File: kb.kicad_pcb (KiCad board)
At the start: 2 copper layers, 203.2 x 106.4 mm, 182 parts, among them J1 Conn_01x04_Female, J2 10029449-001RLF, SW1 RotaryEncoder_Switch, U1 Pico, U2 SN74AHCT125D

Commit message: fixing sk6812s
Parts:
- moved J1 13.1 mm to (87.6, 37.9)
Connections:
- D101 pad 1: Net-(D101-Pad1) -> +5V
- D101 pad 2: GND -> Net-(D101-Pad2)
- D101 pad 3: /RGB_5V -> GND
- D101 pad 4: +5V -> /RGB_5V
- D102 pad 1: Net-(D102-Pad1) -> +5V
- D102 pad 2: GND -> Net-(D102-Pad2)
- D102 pad 3: Net-(D101-Pad1) -> GND
- D102 pad 4: +5V -> Net-(D101-Pad2)
- D103 pad 1: Net-(D103-Pad1) -> +5V
- D103 pad 2: GND -> Net-(D103-Pad2)
- D103 pad 3: Net-(D102-Pad1) -> GND
- D103 pad 4: +5V -> Net-(D102-Pad2)
- D104 pad 1: Net-(D104-Pad1) -> +5V
- D104 pad 2: GND -> Net-(D104-Pad2)
- D104 pad 3: Net-(D103-Pad1) -> GND
- D104 pad 4: +5V -> Net-(D103-Pad2)
- D105 pad 1: Net-(D105-Pad1) -> +5V
- D105 pad 2: GND -> Net-(D105-Pad2)
- D105 pad 3: Net-(D104-Pad1) -> GND
- D105 pad 4: +5V -> Net-(D104-Pad2)
- D106 pad 1: Net-(D106-Pad1) -> +5V
- D106 pad 2: GND -> Net-(D106-Pad2)
- D106 pad 3: Net-(D105-Pad1) -> GND
- D106 pad 4: +5V -> Net-(D105-Pad2)
- D107 pad 1: Net-(D107-Pad1) -> +5V
- D107 pad 2: GND -> Net-(D107-Pad2)
- D107 pad 3: Net-(D106-Pad1) -> GND
- D107 pad 4: +5V -> Net-(D106-Pad2)
- D108 pad 1: Net-(D108-Pad1) -> +5V
- D108 pad 2: GND -> Net-(D108-Pad2)
- D108 pad 3: Net-(D107-Pad1) -> GND
- D108 pad 4: +5V -> Net-(D107-Pad2)
- D109 pad 1: Net-(D109-Pad1) -> +5V
- D109 pad 2: GND -> Net-(D109-Pad2)
- D109 pad 3: Net-(D109-Pad3) -> GND
- D109 pad 4: +5V -> Net-(D109-Pad4)
- D110 pad 1: Net-(D110-Pad1) -> +5V
- D110 pad 2: GND -> Net-(D110-Pad2)
- D110 pad 3: Net-(D109-Pad1) -> GND
- D110 pad 4: +5V -> Net-(D109-Pad2)
- D111 pad 1: Net-(D111-Pad1) -> +5V
- D111 pad 2: GND -> Net-(D111-Pad2)
- D111 pad 3: Net-(D110-Pad1) -> GND
- D111 pad 4: +5V -> Net-(D110-Pad2)
- D112 pad 1: Net-(D112-Pad1) -> +5V
- D112 pad 2: GND -> Net-(D112-Pad2)
- D112 pad 3: Net-(D111-Pad1) -> GND
- D112 pad 4: +5V -> Net-(D111-Pad2)
- D113 pad 1: Net-(D113-Pad1) -> +5V
- D113 pad 2: GND -> Net-(D113-Pad2)
- D113 pad 3: Net-(D112-Pad1) -> GND
- D113 pad 4: +5V -> Net-(D112-Pad2)
- D114 pad 1: Net-(D114-Pad1) -> +5V
- D114 pad 2: GND -> Net-(D114-Pad2)
- D114 pad 3: Net-(D113-Pad1) -> GND
- D114 pad 4: +5V -> Net-(D113-Pad2)
- D115 pad 1: Net-(D115-Pad1) -> +5V
- D115 pad 2: GND -> Net-(D115-Pad2)
- D115 pad 3: Net-(D114-Pad1) -> GND
- D115 pad 4: +5V -> Net-(D114-Pad2)
- D116 pad 1: Net-(D116-Pad1) -> +5V
- D116 pad 2: GND -> Net-(D116-Pad2)
- D116 pad 3: Net-(D115-Pad1) -> GND
- D116 pad 4: +5V -> Net-(D115-Pad2)
- D117 pad 1: Net-(D117-Pad1) -> +5V
- D117 pad 2: GND -> Net-(D117-Pad2)
- D117 pad 3: Net-(D116-Pad1) -> GND
- D117 pad 4: +5V -> Net-(D116-Pad2)
- D118 pad 1: Net-(D118-Pad1) -> +5V
- D118 pad 2: GND -> Net-(D118-Pad2)
- D118 pad 3: Net-(D117-Pad1) -> GND
- D118 pad 4: +5V -> Net-(D117-Pad2)
- D119 pad 1: Net-(D119-Pad1) -> +5V
- D119 pad 2: GND -> Net-(D119-Pad2)
- D119 pad 3: Net-(D118-Pad1) -> GND
- D119 pad 4: +5V -> Net-(D118-Pad2)
- D120 pad 1: Net-(D120-Pad1) -> +5V
- D120 pad 2: GND -> Net-(D120-Pad2)
- D120 pad 3: Net-(D119-Pad1) -> GND
- D120 pad 4: +5V -> Net-(D119-Pad2)
- D121 pad 1: Net-(D121-Pad1) -> +5V
- D121 pad 2: GND -> Net-(D121-Pad2)
- D121 pad 3: Net-(D120-Pad1) -> GND
- D121 pad 4: +5V -> Net-(D120-Pad2)
- D122 pad 1: Net-(D122-Pad1) -> +5V
- D122 pad 2: GND -> Net-(D122-Pad2)
- D122 pad 3: Net-(D121-Pad1) -> GND
- D122 pad 4: +5V -> Net-(D121-Pad2)
- D123 pad 1: Net-(D123-Pad1) -> +5V
- D123 pad 2: GND -> Net-(D123-Pad2)
- D123 pad 3: Net-(D122-Pad1) -> GND
- D123 pad 4: +5V -> Net-(D122-Pad2)
- D124 pad 1: Net-(D124-Pad1) -> +5V
- D124 pad 2: GND -> Net-(D124-Pad2)
- D124 pad 3: Net-(D123-Pad1) -> GND
- D124 pad 4: +5V -> Net-(D123-Pad2)
- D125 pad 1: Net-(D125-Pad1) -> +5V
- D125 pad 2: GND -> Net-(D125-Pad2)
- D125 pad 3: Net-(D124-Pad1) -> GND
- D125 pad 4: +5V -> Net-(D124-Pad2)
- D126 pad 1: Net-(D126-Pad1) -> +5V
- D126 pad 2: GND -> Net-(D126-Pad2)
- D126 pad 3: Net-(D125-Pad1) -> GND
- D126 pad 4: +5V -> Net-(D125-Pad2)
- D127 pad 1: Net-(D127-Pad1) -> +5V
- D127 pad 2: GND -> Net-(D127-Pad2)
- D127 pad 3: Net-(D126-Pad1) -> GND
- D127 pad 4: +5V -> Net-(D126-Pad2)
- D128 pad 1: Net-(D128-Pad1) -> +5V
- D128 pad 2: GND -> Net-(D128-Pad2)
- D128 pad 3: Net-(D127-Pad1) -> GND
- D128 pad 4: +5V -> Net-(D127-Pad2)
- D129 pad 1: Net-(D129-Pad1) -> +5V
- D129 pad 2: GND -> Net-(D129-Pad2)
- D129 pad 3: Net-(D128-Pad1) -> GND
- D129 pad 4: +5V -> Net-(D128-Pad2)
- D130 pad 1: Net-(D130-Pad1) -> +5V
- D130 pad 2: GND -> Net-(D130-Pad2)
- D130 pad 3: Net-(D129-Pad1) -> GND
- D130 pad 4: +5V -> Net-(D129-Pad2)
- D131 pad 1: Net-(D131-Pad1) -> +5V
- D131 pad 2: GND -> Net-(D131-Pad2)
- D131 pad 3: Net-(D130-Pad1) -> GND
- D131 pad 4: +5V -> Net-(D130-Pad2)
- D132 pad 1: Net-(D132-Pad1) -> +5V
- D132 pad 2: GND -> Net-(D132-Pad2)
- D132 pad 3: Net-(D131-Pad1) -> GND
- D132 pad 4: +5V -> Net-(D131-Pad2)
- D133 pad 1: Net-(D133-Pad1) -> +5V
- D133 pad 2: GND -> Net-(D133-Pad2)
- D133 pad 3: Net-(D132-Pad1) -> GND
- D133 pad 4: +5V -> Net-(D132-Pad2)
- D134 pad 1: Net-(D134-Pad1) -> +5V
- D134 pad 2: GND -> Net-(D134-Pad2)
- D134 pad 3: Net-(D133-Pad1) -> GND
- D134 pad 4: +5V -> Net-(D133-Pad2)
- D135 pad 1: Net-(D135-Pad1) -> +5V
- D135 pad 2: GND -> Net-(D135-Pad2)
- D135 pad 3: Net-(D134-Pad1) -> GND
- D135 pad 4: +5V -> Net-(D134-Pad2)
- D136 pad 1: Net-(D136-Pad1) -> +5V
- D136 pad 2: GND -> Net-(D136-Pad2)
- D136 pad 3: Net-(D135-Pad1) -> GND
- D136 pad 4: +5V -> Net-(D135-Pad2)
- D137 pad 1: Net-(D137-Pad1) -> +5V
- D137 pad 2: GND -> Net-(D137-Pad2)
- D137 pad 3: Net-(D136-Pad1) -> GND
- D137 pad 4: +5V -> Net-(D136-Pad2)
- D138 pad 1: Net-(D138-Pad1) -> +5V
- D138 pad 2: GND -> Net-(D138-Pad2)
- D138 pad 3: Net-(D137-Pad1) -> GND
- D138 pad 4: +5V -> Net-(D137-Pad2)
- D139 pad 1: Net-(D139-Pad1) -> +5V
- D139 pad 2: GND -> Net-(D139-Pad2)
- D139 pad 3: Net-(D138-Pad1) -> GND
- D139 pad 4: +5V -> Net-(D138-Pad2)
- D140 pad 1: Net-(D140-Pad1) -> +5V
- D140 pad 2: GND -> Net-(D140-Pad2)
- D140 pad 3: Net-(D139-Pad1) -> GND
- D140 pad 4: +5V -> Net-(D139-Pad2)
- D141 pad 1: Net-(D141-Pad1) -> +5V
- D141 pad 2: GND -> Net-(D141-Pad2)
- D141 pad 3: Net-(D140-Pad1) -> GND
- D141 pad 4: +5V -> Net-(D140-Pad2)
- D142 pad 1: Net-(D142-Pad1) -> +5V
- D142 pad 2: GND -> Net-(D142-Pad2)
- D142 pad 3: Net-(D141-Pad1) -> GND
- D142 pad 4: +5V -> Net-(D141-Pad2)
- D143 pad 1: /RGB_TO_RIGHT -> +5V
- D143 pad 2: GND -> /RGB_TO_RIGHT
- D143 pad 3: Net-(D142-Pad1) -> GND
- D143 pad 4: +5V -> Net-(D142-Pad2)
- D144 pad 1: Net-(D109-Pad3) -> +5V
- D144 pad 2: GND -> Net-(D109-Pad4)
- D144 pad 3: Net-(D108-Pad1) -> GND
- D144 pad 4: +5V -> Net-(D108-Pad2)
- J2 pad 1: unconnected-(J2-Pad1) -> /ROW9
- J2 pad 10: unconnected-(J2-Pad10) -> /COL4
- J2 pad 11: unconnected-(J2-Pad11) -> /COL5
- J2 pad 12: unconnected-(J2-Pad12) -> /COL6
- J2 pad 13: unconnected-(J2-Pad13) -> /COL7
- J2 pad 14: unconnected-(J2-Pad14) -> /COL8
- J2 pad 15: /ENC_R1 -> /ENC_R2
- J2 pad 16: /ENC_R2 -> /ENC_R1
- J2 pad 2: unconnected-(J2-Pad2) -> /ROW8
- J2 pad 3: unconnected-(J2-Pad3) -> /ROW7
- J2 pad 4: unconnected-(J2-Pad4) -> /ROW6
- J2 pad 5: unconnected-(J2-Pad5) -> /ROW5
- J2 pad 6: unconnected-(J2-Pad6) -> /COL0
- J2 pad 7: unconnected-(J2-Pad7) -> /COL1
- J2 pad 8: unconnected-(J2-Pad8) -> /COL2
- J2 pad 9: unconnected-(J2-Pad9) -> /COL3
- U1 pad 10: /ENC_R2 -> /ENC_R1
- U1 pad 11: /ENC_R1 -> /ENC_R2
- U1 pad 21: unconnected-(U1-Pad21) -> /ROW9
- U1 pad 22: unconnected-(U1-Pad22) -> /ROW8
- U1 pad 24: unconnected-(U1-Pad24) -> /ROW7
- U1 pad 25: unconnected-(U1-Pad25) -> /ROW6
- U1 pad 26: unconnected-(U1-Pad26) -> /ROW5
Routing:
- net GND: track 0.00 -> 714.4 mm
- net +5V: track 986.0 -> 321.0 mm
- net Net-(D135-Pad1): track 213.3 -> 0.00 mm
- net Net-(D126-Pad1): track 200.8 -> 0.00 mm
- net Net-(D109-Pad4): track 0.00 -> 199.8 mm
- net Net-(D117-Pad1): track 195.4 -> 0.00 mm
- net Net-(D109-Pad3): track 193.3 -> 0.00 mm
- net Net-(D129-Pad1): track 31.2 -> 0.00 mm
- net Net-(D142-Pad1): track 27.0 -> 0.00 mm
- net Net-(D130-Pad1): track 26.5 -> 0.00 mm
- net Net-(D120-Pad1): track 26.5 -> 0.00 mm
- net Net-(D138-Pad1): track 24.1 -> 0.00 mm
- net Net-(D111-Pad1): track 24.1 -> 0.00 mm
- net Net-(D102-Pad1): track 21.8 -> 0.00 mm
- net Net-(D139-Pad1): track 21.7 -> 0.00 mm
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
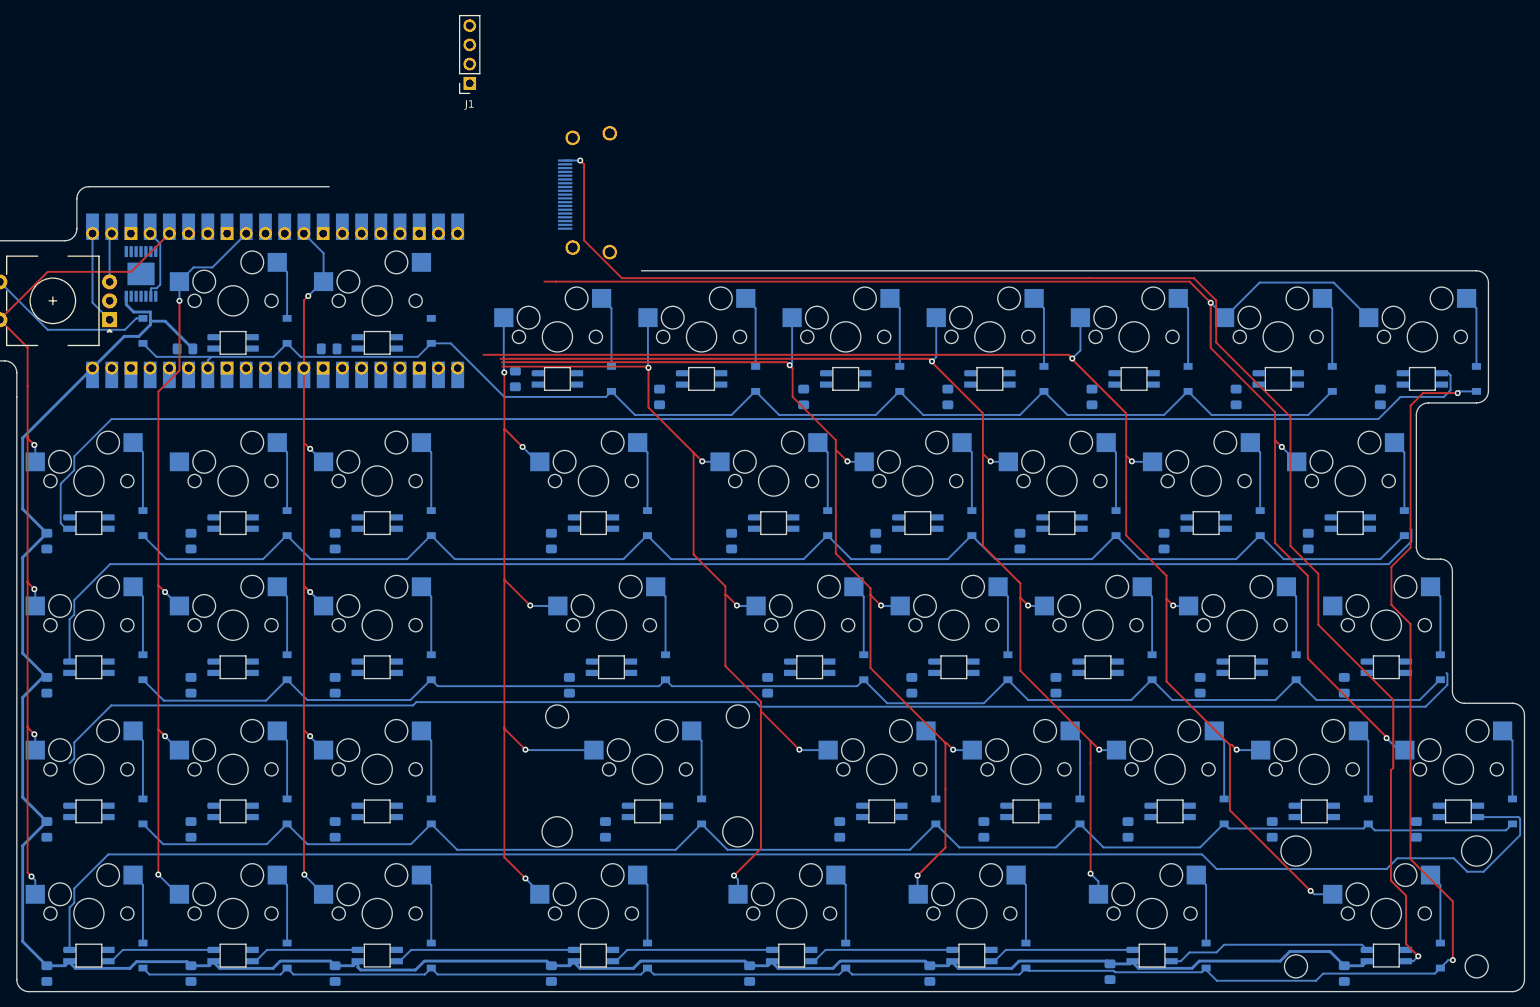
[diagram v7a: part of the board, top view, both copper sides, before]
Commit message: routing hdmi done
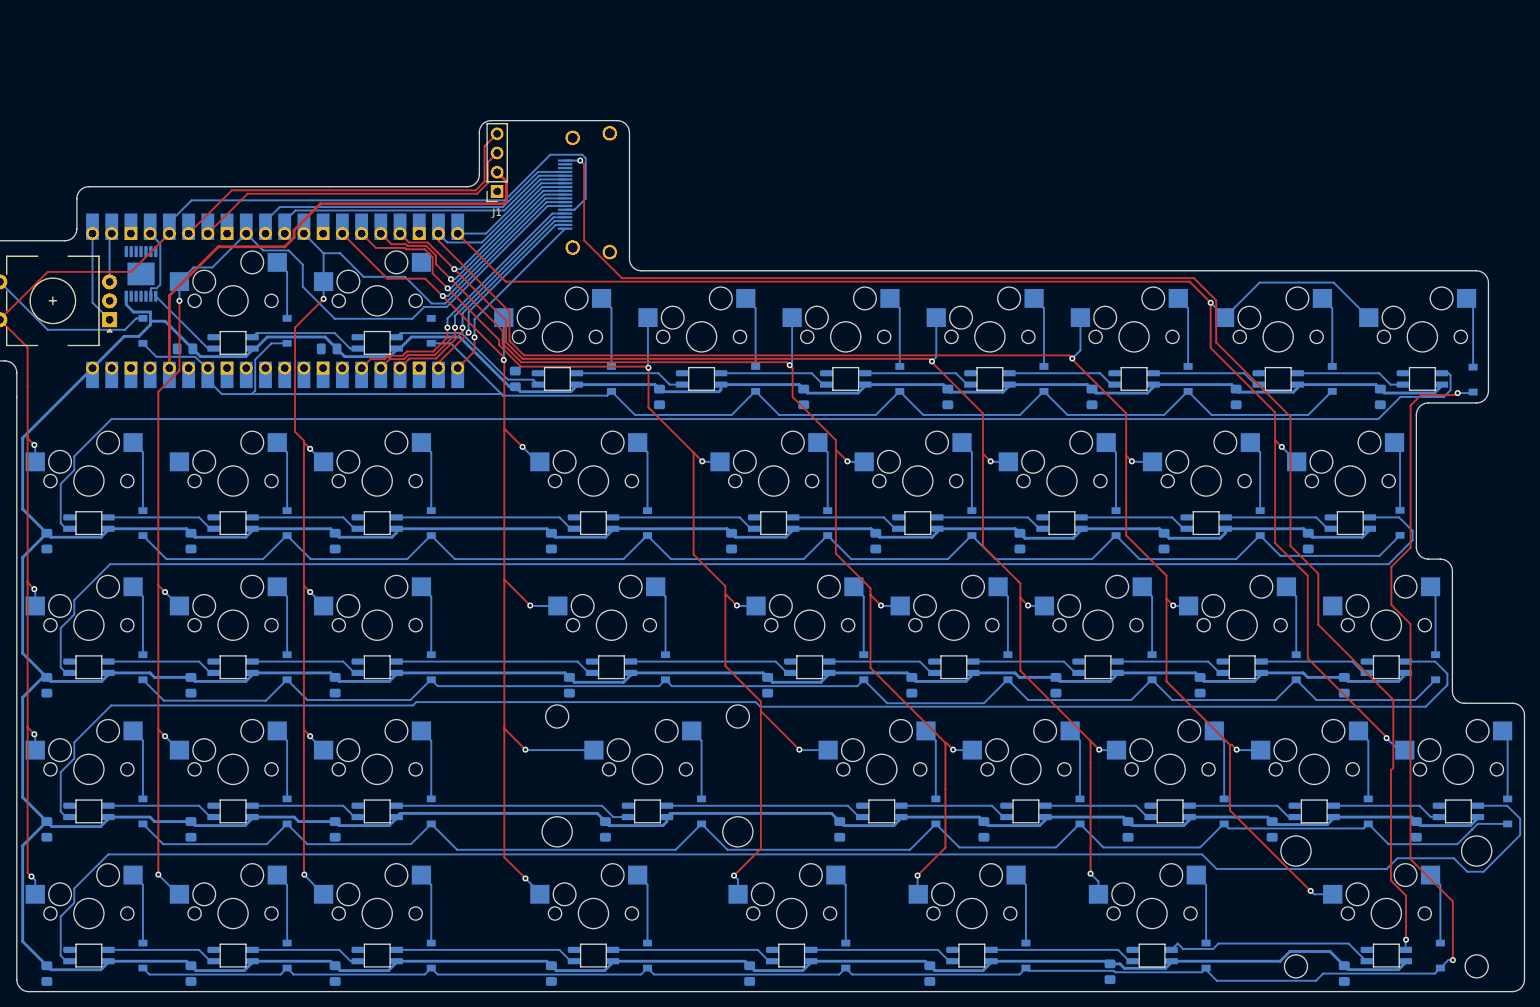
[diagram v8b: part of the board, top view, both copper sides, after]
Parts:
- moved J1 14.7 mm to (91.3, 52.2)
- moved D26 0.64 mm to (215.3, 115.1)
- moved D35 0.64 mm to (224.8, 134.1)
- moved D17 0.57 mm to (210.6, 96.0)
- moved D44 0.45 mm to (220.2, 77.1)
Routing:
- net +5V: track 321.0 -> 1056.7 mm
- net GND: track 714.4 -> 0.00 mm
- net Net-(D135-Pad2): track 0.00 -> 216.7 mm
- net Net-(D126-Pad2): track 0.00 -> 204.1 mm
- net Net-(D117-Pad2): track 0.00 -> 198.9 mm
- net /COL0: track 115.9 -> 185.0 mm
- net +3V3: track 0.00 -> 64.2 mm
- net /COL1: track 102.7 -> 157.4 mm
- net /COL3: track 106.3 -> 156.3 mm, vias 5 -> 6
- net /OLED_SDA: track 0.00 -> 49.0 mm
- net /COL4: track 123.1 -> 171.3 mm, vias 5 -> 6
- net /COL5: track 137.5 -> 182.1 mm, vias 5 -> 6
- net /OLED_SCL: track 0.00 -> 44.2 mm
- net /ENC_R1: track 0.00 -> 43.9 mm
- net /ENC_R2: track 0.00 -> 41.2 mm
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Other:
- board size 203.2 x 106.4 mm -> 203.2 x 115.1 mm
